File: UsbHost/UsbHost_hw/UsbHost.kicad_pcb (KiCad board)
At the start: 2 copper layers, 114 x 16 mm, 41 parts

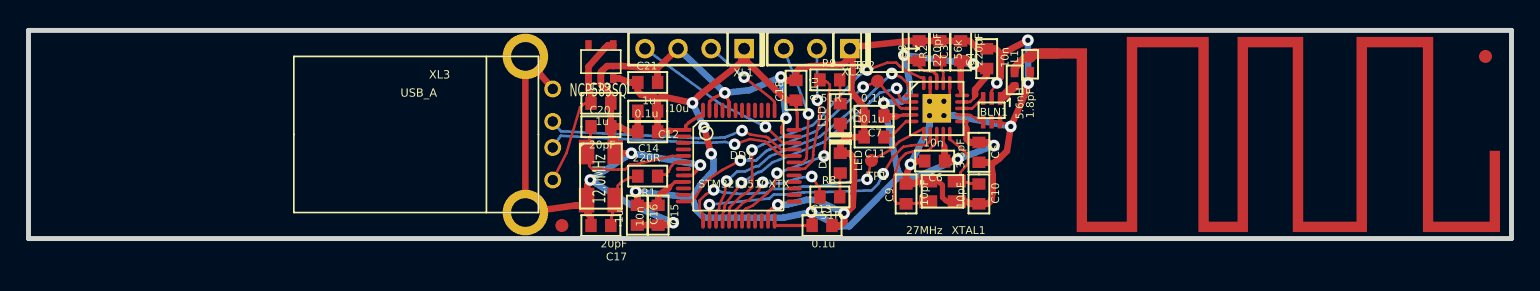
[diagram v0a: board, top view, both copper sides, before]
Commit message: + UsbHaost PCB ready and sent to production
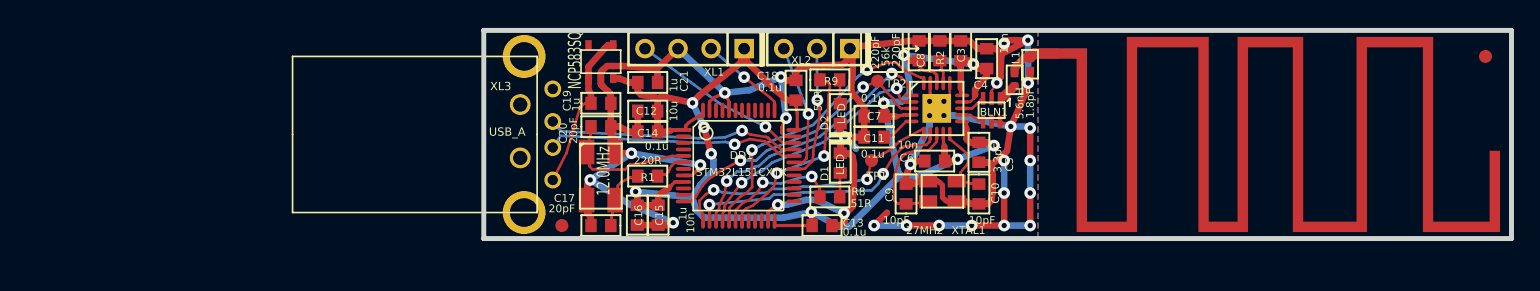
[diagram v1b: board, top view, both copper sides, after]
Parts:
- moved XL3 0.10 mm to (199.1, 181.0)
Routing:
- net GND: track 173.0 -> 185.4 mm, vias 14 -> 27
- added copper zone on B.Cu, net GND
- added copper zone on F.Cu, net GND
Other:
- board size 114 x 16 mm -> 79 x 16 mm
